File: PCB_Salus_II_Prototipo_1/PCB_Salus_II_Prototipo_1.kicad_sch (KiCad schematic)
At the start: 43 parts, among them J1 Servo1, J11 Conector Entrada 5V, J12 Conector 5V, J13 Conector Entrada 7V, J14 Conector Salida 7V, J16 Luz2, J17 Cambios1, J18 Cambios 2, J19 MarchaAtras1, J2 Sensor Giro, J20 MarchaAtras2, J21 Sobrante1, J22 Sobrante2, J23 Arranque1, J24 Arranque2, J25 ControlMotor, J3 Acelerador, J4 Conn_01x05_Pin, J5 Servo2, J6 Antena, J7 SensorGiro, J8 Luz1, K1 Rele 5V, K2 Rele 7V, K3 Arranque, Q1 IO25, Q2 IO26, Q3 IO27, Q4 IO14, U1 ESP32-DEVKITC-32D, U2 RASPBERRY_PI_4B_4GB

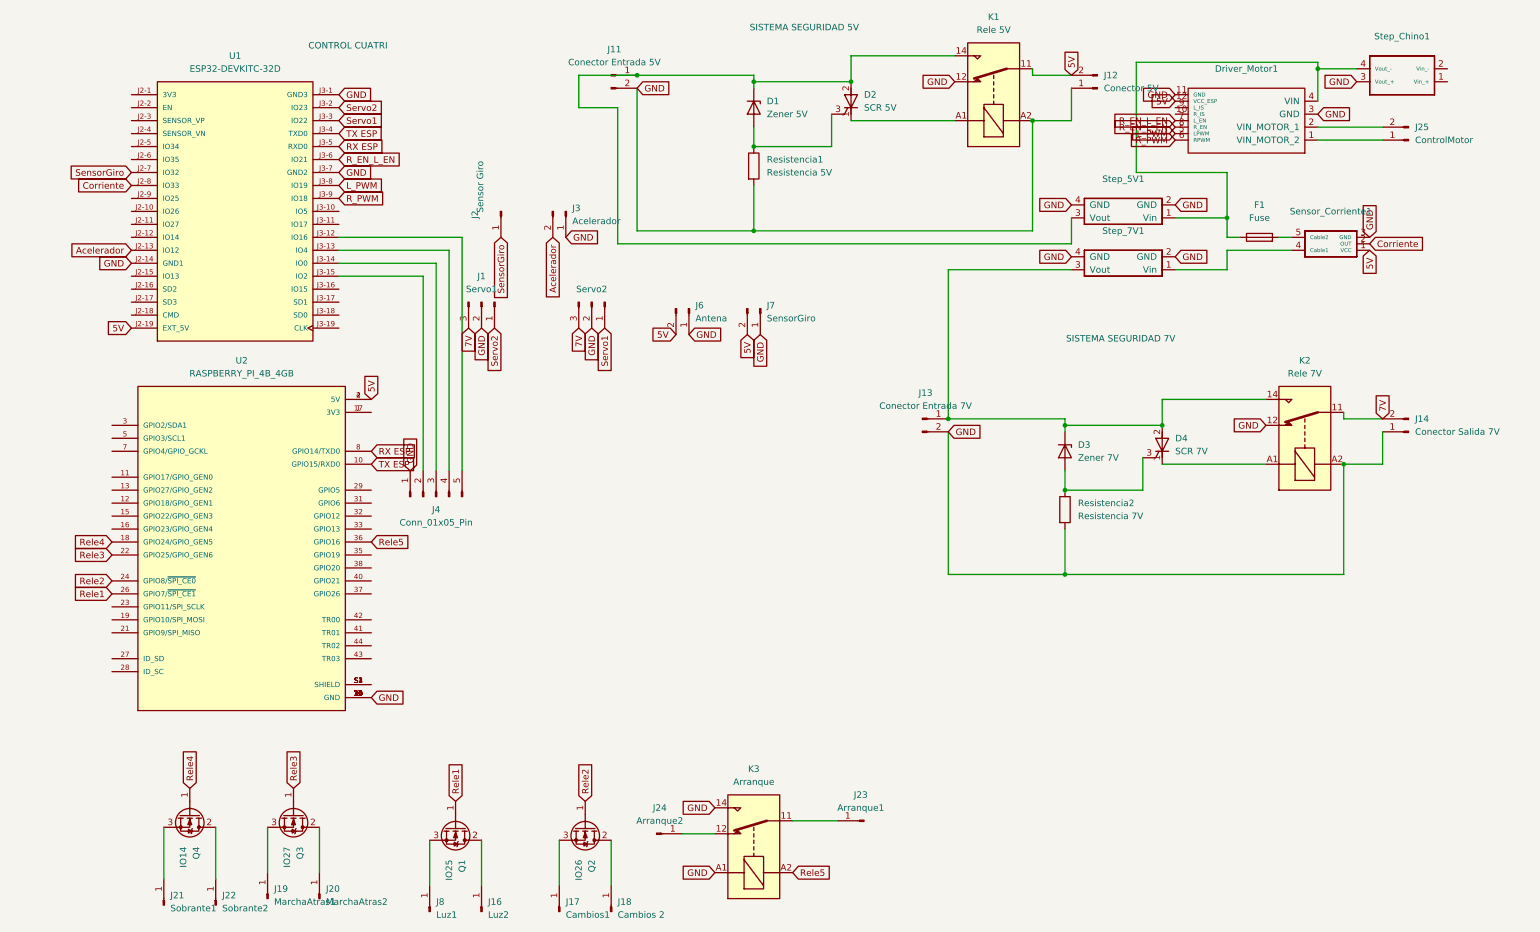
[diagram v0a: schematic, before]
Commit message: Modifique la fuente de alimentacion de sensor de Corriente y de giro
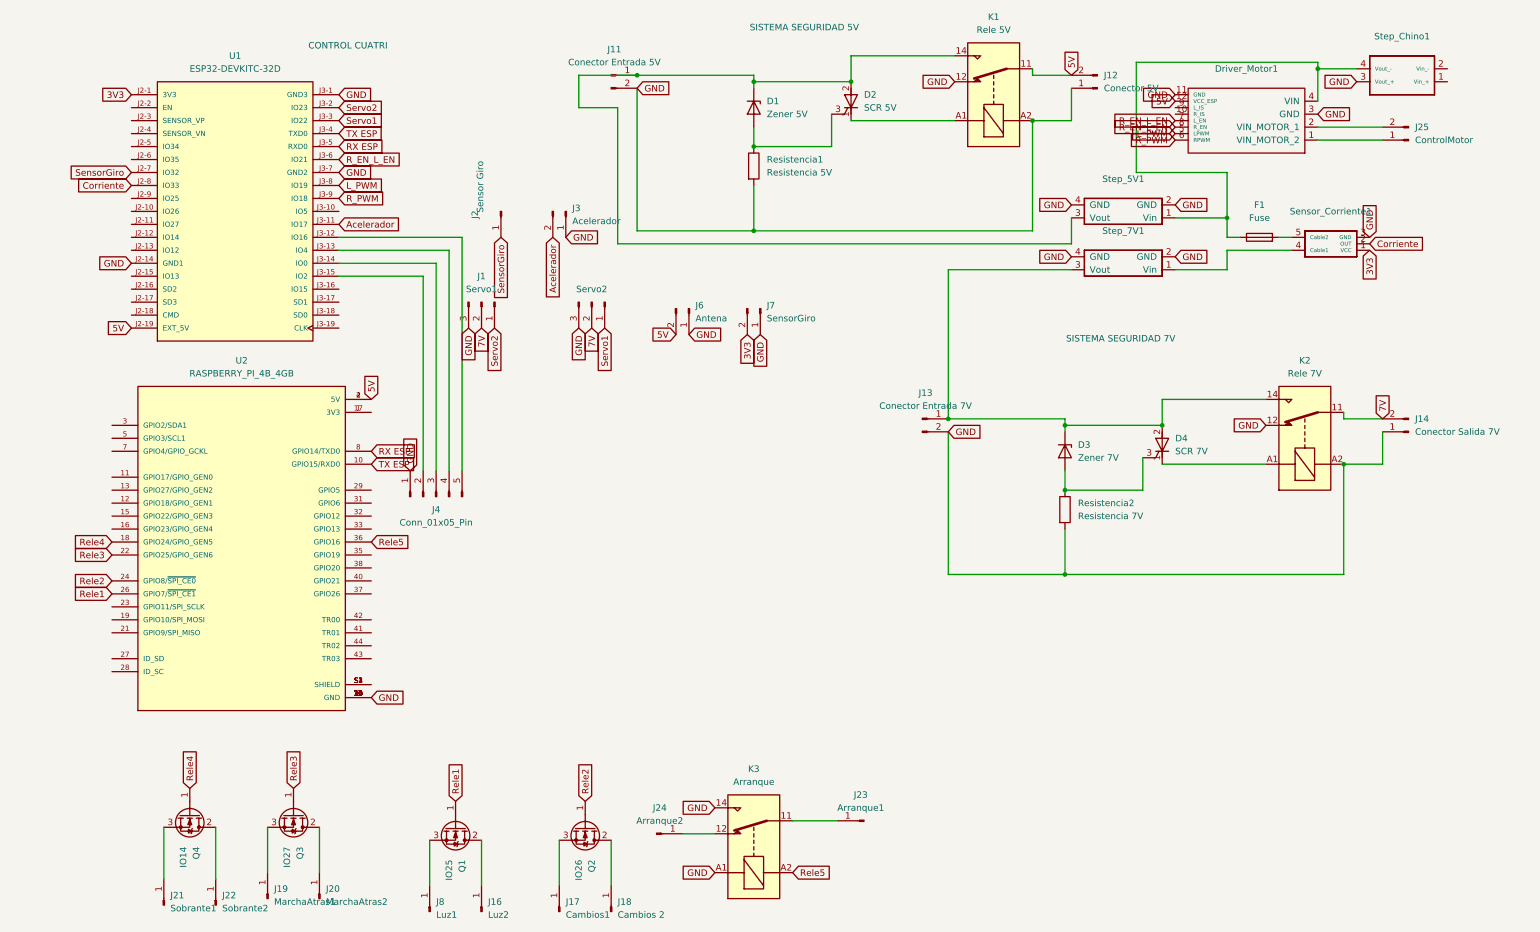
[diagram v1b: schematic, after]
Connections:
- net 5V: no longer J7.2 (Pin_2), Sensor_Corriente1.1 (VCC)
- net 7V: now also J1.2 (Pin_2), J5.2 (Pin_2); no longer J1.3 (Pin_3), J5.3 (Pin_3)
- net Acelerador: now also U1.J3-11 (IO17); no longer U1.J2-13 (IO12)
- net GND: now also J1.3 (Pin_3), J5.3 (Pin_3); no longer J1.2 (Pin_2), J5.2 (Pin_2)
- net 3V3: now reaches U1.J2-1 (3V3)
- net 3V3: now also J7.2 (Pin_2), Sensor_Corriente1.1 (VCC)

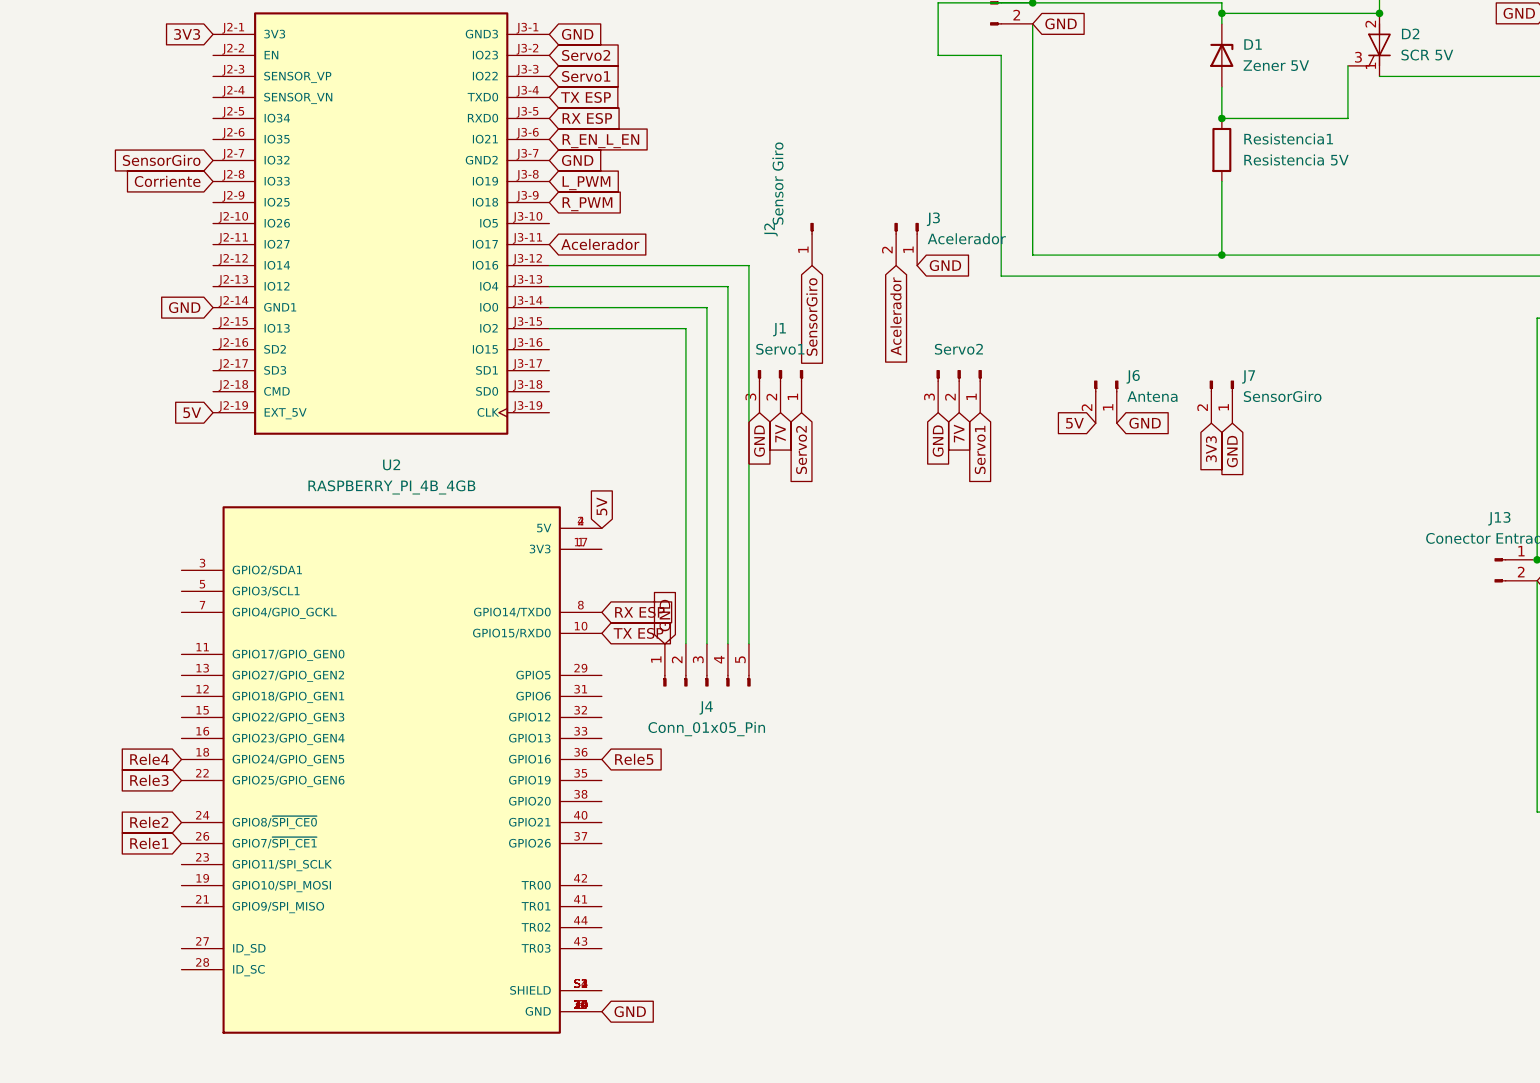
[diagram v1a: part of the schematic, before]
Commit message: Se agrego sensores ultrasonidos
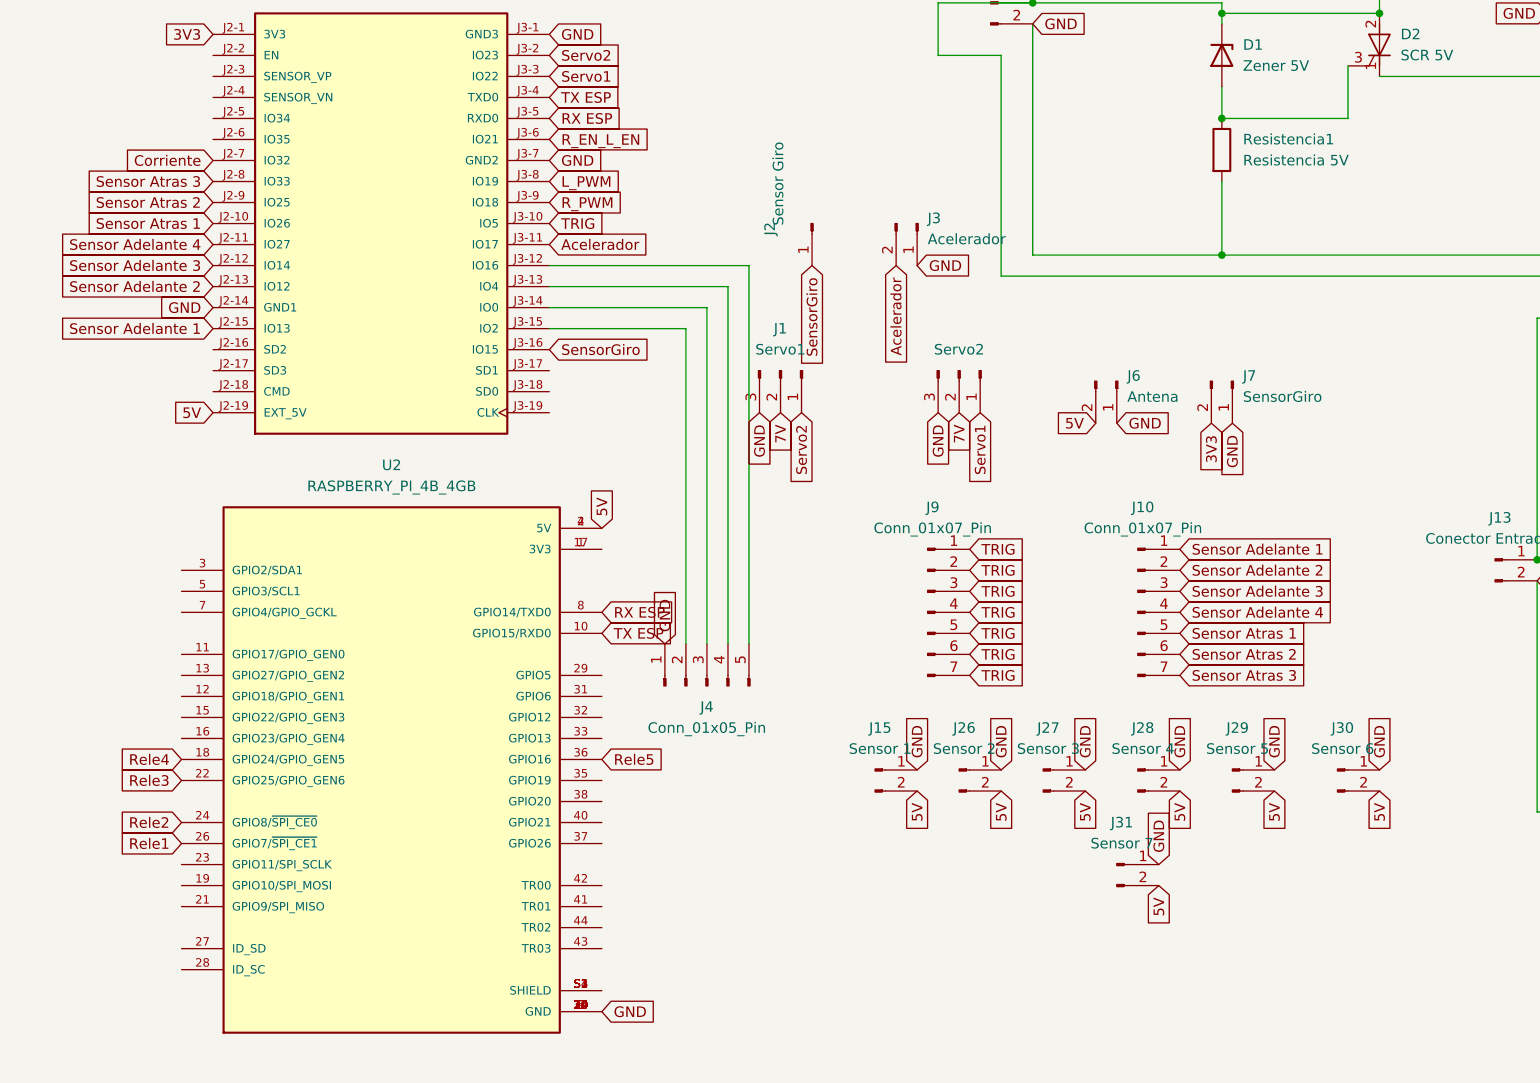
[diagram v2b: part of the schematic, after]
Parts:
- added J10, J9: Conn_01x07_Pin, Connector_PinHeader_2.54mm:PinHeader_1x07_P2.54mm_Vertical, symbol Connector:Conn_01x07_Pin
- added J15: Sensor 1, Connector_PinHeader_2.54mm:PinHeader_1x02_P2.54mm_Vertical, symbol Connector:Conn_01x02_Pin
- added J26: Sensor 2, Connector_PinHeader_2.54mm:PinHeader_1x02_P2.54mm_Vertical, symbol Connector:Conn_01x02_Pin
- added J27: Sensor 3, Connector_PinHeader_2.54mm:PinHeader_1x02_P2.54mm_Vertical, symbol Connector:Conn_01x02_Pin
- added J28: Sensor 4, Connector_PinHeader_2.54mm:PinHeader_1x02_P2.54mm_Vertical, symbol Connector:Conn_01x02_Pin
- added J29: Sensor 5, Connector_PinHeader_2.54mm:PinHeader_1x02_P2.54mm_Vertical, symbol Connector:Conn_01x02_Pin
- added J30: Sensor 6, Connector_PinHeader_2.54mm:PinHeader_1x02_P2.54mm_Vertical, symbol Connector:Conn_01x02_Pin
- added J31: Sensor 7, Connector_PinHeader_2.54mm:PinHeader_1x02_P2.54mm_Vertical, symbol Connector:Conn_01x02_Pin
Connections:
- net 5V: now also J15.2 (Pin_2), J26.2 (Pin_2), J27.2 (Pin_2), J28.2 (Pin_2), J29.2 (Pin_2), J30.2 (Pin_2), J31.2 (Pin_2)
- net Corriente: now also U1.J2-7 (IO32); no longer U1.J2-8 (IO33)
- net GND: now also J15.1 (Pin_1), J26.1 (Pin_1), J27.1 (Pin_1), J28.1 (Pin_1), J29.1 (Pin_1), J30.1 (Pin_1), J31.1 (Pin_1)
- net SensorGiro: now also U1.J3-16 (IO15); no longer U1.J2-7 (IO32)
- net Sensor Atras 1: now reaches U1.J2-10 (IO26)
- net Sensor Atras 1: now also J10.5 (Pin_5)
- net Sensor Adelante 4: now reaches U1.J2-11 (IO27)
- net Sensor Adelante 4: now also J10.4 (Pin_4)
- net Sensor Adelante 3: now reaches U1.J2-12 (IO14)
- net Sensor Adelante 3: now also J10.3 (Pin_3)
- net Sensor Adelante 2: now reaches U1.J2-13 (IO12)
- net Sensor Adelante 2: now also J10.2 (Pin_2)
- net Sensor Adelante 1: now reaches U1.J2-15 (IO13)
- net Sensor Adelante 1: now also J10.1 (Pin_1)
- net Sensor Atras 2: now reaches U1.J2-9 (IO25)
- net Sensor Atras 2: now also J10.6 (Pin_6)
- net TRIG: now reaches U1.J3-10 (IO5)
- net TRIG: now also J9.1 (Pin_1), J9.2 (Pin_2), J9.3 (Pin_3), J9.4 (Pin_4), J9.5 (Pin_5), J9.6 (Pin_6), J9.7 (Pin_7)
- new net Sensor Atras 3: J10.7 (Pin_7), U1.J2-8 (IO33)
